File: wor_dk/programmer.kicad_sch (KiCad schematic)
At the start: 44 parts, among them J501 SWD, J502 USB_C_Receptacle_USB2.0_16P, J503 SWD, Q501 BSS84, SW501 SW_Push, U501 TLV1117-33, U502 LPC11U35FHI33_501, Y501 12MHz

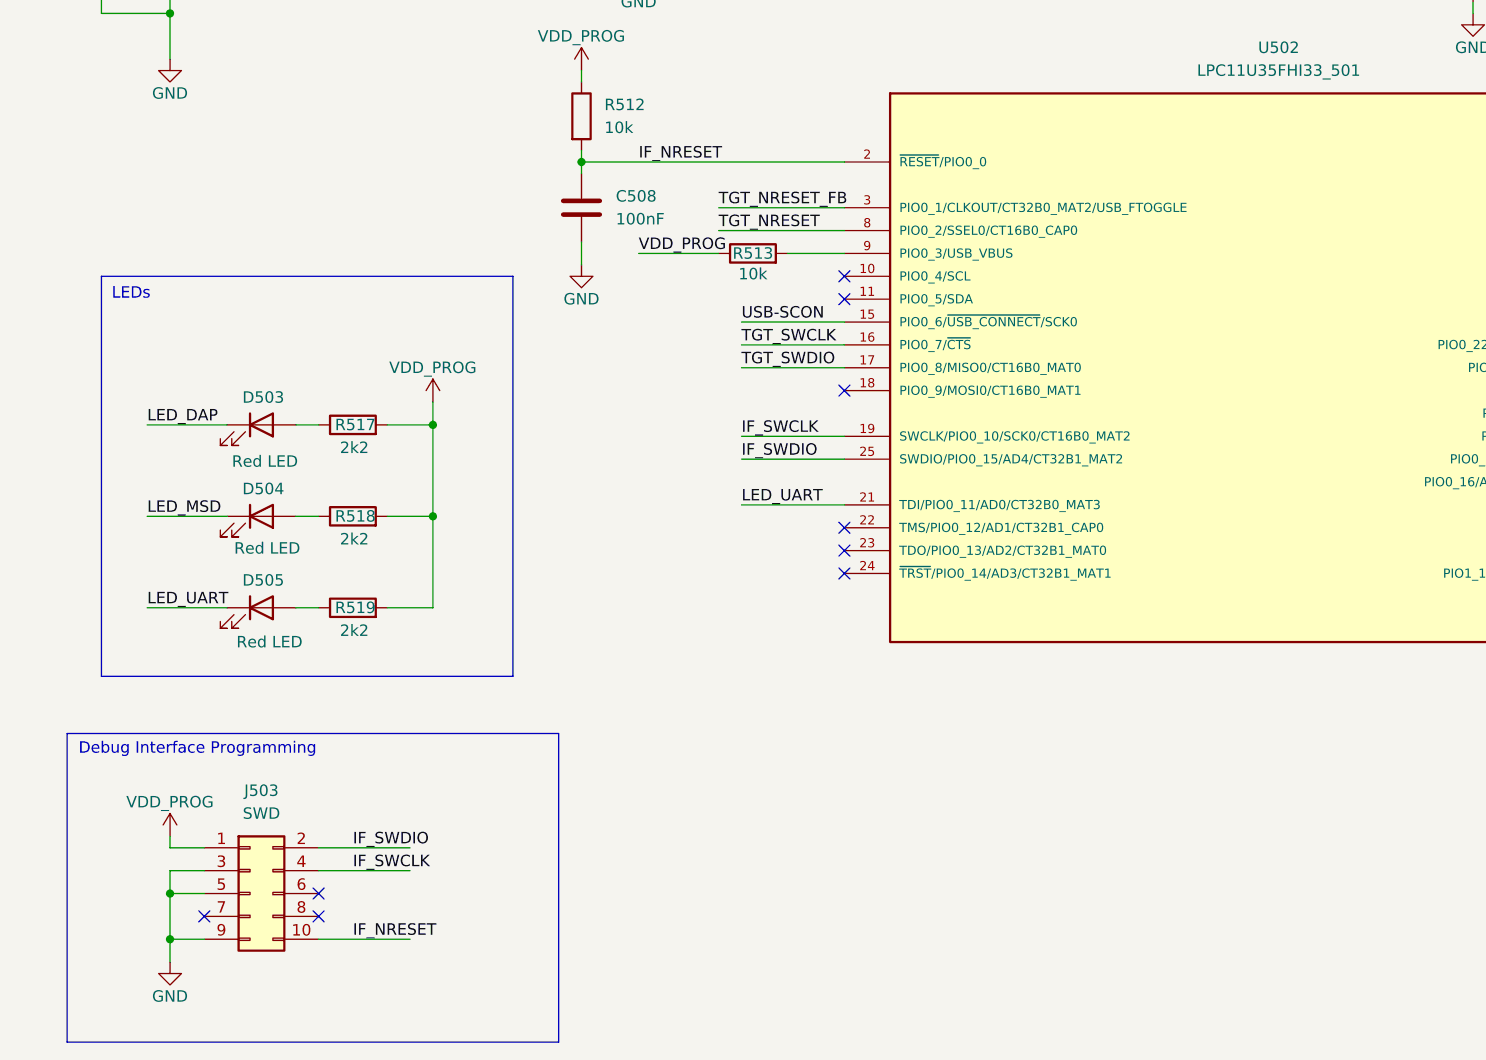
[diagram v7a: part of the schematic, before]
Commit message: wor_dk: schematic: add reset buttons for FT232 & LPC11U35
This is just for convenience.
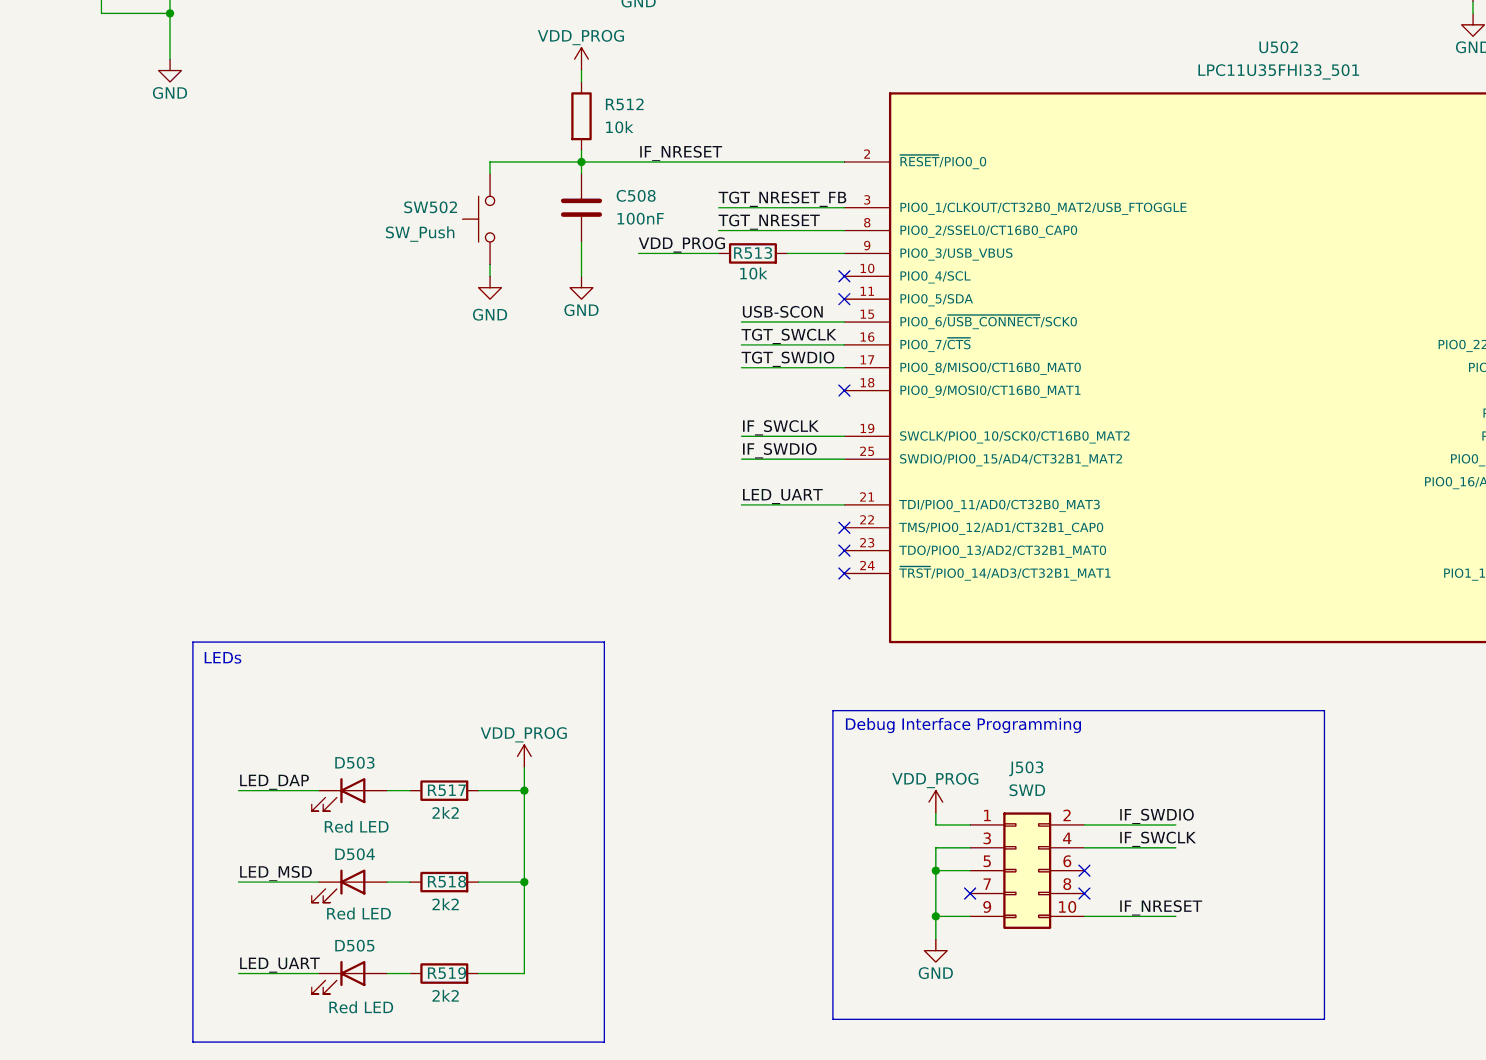
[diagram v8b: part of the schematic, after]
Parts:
- added SW502: SW_Push, Button_Switch_SMD:SW_SPST_PTS810, symbol Switch:SW_Push
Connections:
- net GND: now also SW502.1
- net IF_NRESET: now also SW502.2
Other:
- moved on the sheet: D503, D504, D505, J503, R517, R518, R519
